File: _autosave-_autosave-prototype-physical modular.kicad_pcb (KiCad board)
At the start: 2 copper layers, 100 x 164 mm, 183 parts, among them CON1 BARREL_JACK, CON2 SD_Card_SEEEDOPL, IC1 ATMEGA2560-A, P1 POWER, P10 PC, P11 CONN_UART, P12 PJ, P15 PH, P16 PF, P18 3VI2C, P19 PIGPIO, P20 MIDI_IN, P21 MIDI_OUT, P22 BUSTI, P23 BUSTO, P3 SPI, P7 PA, Q1 BSS138, Q2 BSS138, Q3 BSS138, Q4 BSS138, Q5 BSS138, Q6 BSS138, SW1 SW_PUSH, SW10 SW_PUSH, SW11 SW_PUSH, SW12 SW_PUSH, SW13 SW_PUSH, SW14 SW_PUSH, SW2 ROTARY_ENCODER_SWITCH, SW3 SW_PUSH, SW4 SW_PUSH, SW5 SW_PUSH, SW6 SW_PUSH, SW7 SW_PUSH, SW8 SW_PUSH, SW9 SW_PUSH, U1 NCP1117ST50T3G, U2 6N138, Y1 16MHz

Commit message: new go at routing
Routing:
- net GND: track 0.00 -> 995.8 mm, vias 0 -> 29
- net +5V: track 0.00 -> 813.9 mm, vias 0 -> 44
- net /BUS_COM: track 0.00 -> 289.4 mm, vias 0 -> 3
- net /TX3: track 0.00 -> 251.4 mm, vias 0 -> 3
- net /MUXAX0: track 0.00 -> 238.7 mm, vias 0 -> 5
- net /MUXAX1: track 0.00 -> 223.4 mm, vias 0 -> 8
- net /MUXAX3: track 0.00 -> 213.7 mm, vias 0 -> 3
- net /MUXBX6: track 0.00 -> 190.4 mm, vias 0 -> 4
- net Net-(IC1-Pad65): track 0.00 -> 185.4 mm, vias 0 -> 3
- net /MUXAX2: track 0.00 -> 182.6 mm, vias 0 -> 4
- net /MUXAX4: track 0.00 -> 175.1 mm, vias 0 -> 1
- net /MUXBX5: track 0.00 -> 148.0 mm, vias 0 -> 2
- net /MUXBX4: track 0.00 -> 143.8 mm, vias 0 -> 3
- net /MUXBX1: track 0.00 -> 141.2 mm, vias 0 -> 6
- net /BUSTO_CONN: track 0.00 -> 140.0 mm, vias 0 -> 2
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
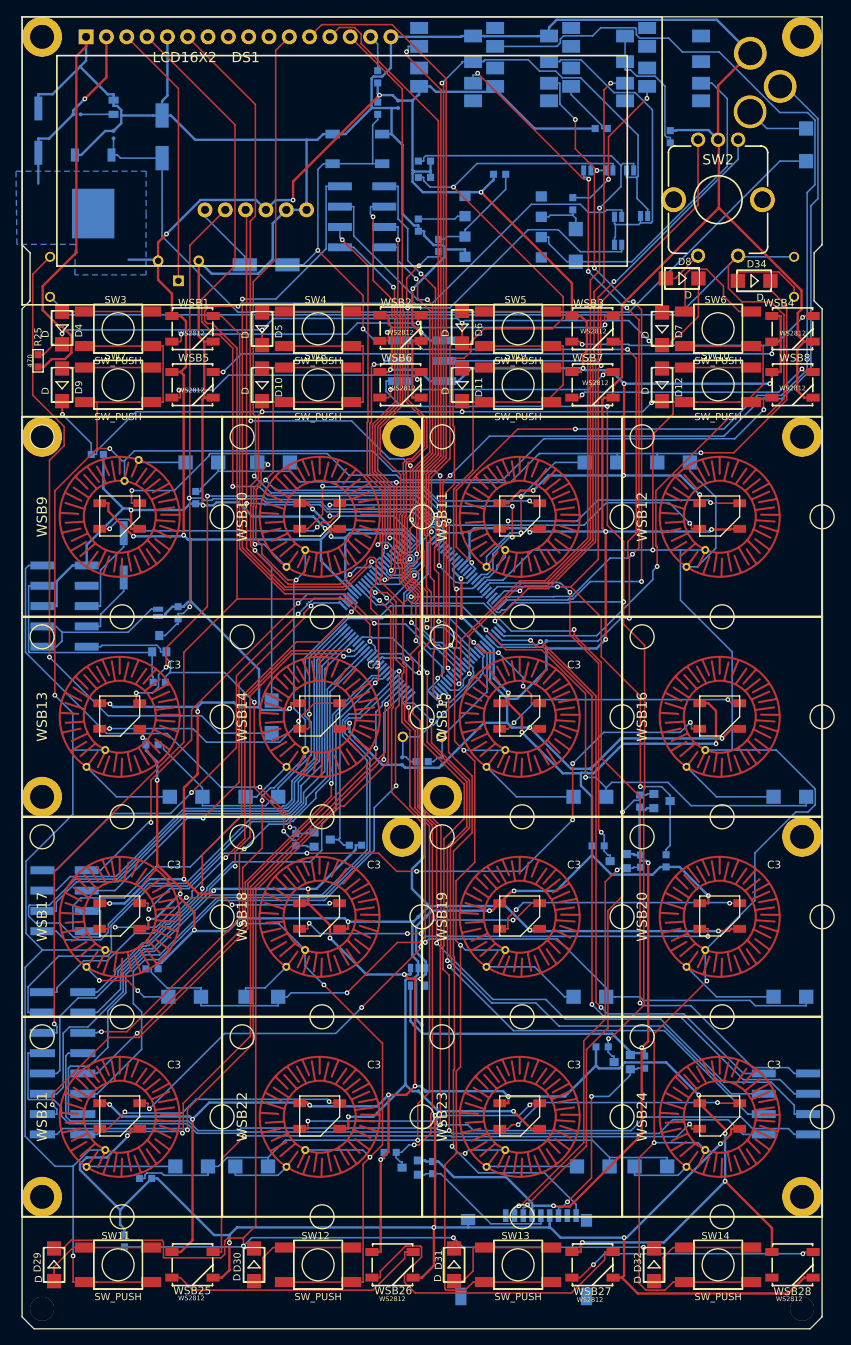
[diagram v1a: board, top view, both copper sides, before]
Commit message: move controller and hybrid firmware to virtualModular project
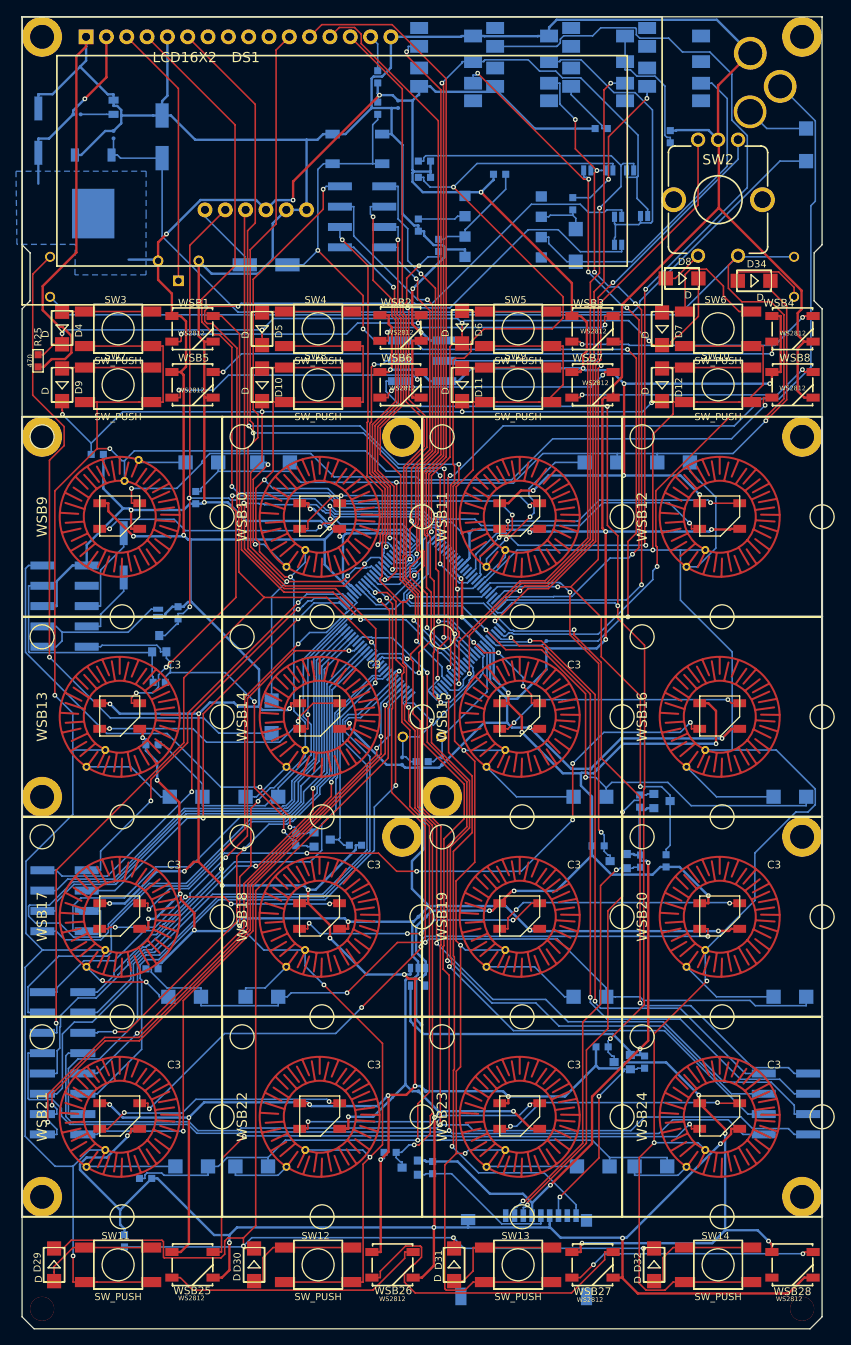
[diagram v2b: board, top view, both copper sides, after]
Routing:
- net /BUSTO_CONN: track 140.0 -> 124.6 mm
- net /PI5vRX0: track 129.9 -> 121.4 mm
- net Net-(IC1-Pad53): track 84.8 -> 78.9 mm
- net /MUXBX1: track 141.2 -> 136.2 mm
- net Net-(IC1-Pad68): track 67.0 -> 63.3 mm
- net +3V3: track 118.2 -> 114.8 mm
- net Net-(IC1-Pad91): track 75.8 -> 72.5 mm
- net /LCD1: track 103.1 -> 106.2 mm
- net GND: track 995.8 -> 993.5 mm
- net Net-(WSB10-Pad2): track 35.2 -> 33.0 mm
- net Net-(IC1-Pad65): track 185.4 -> 183.5 mm
- net +5V: track 813.9 -> 812.1 mm
- net /LCD4: track 93.1 -> 92.1 mm
- net /3vSPI_MISO: track 25.4 -> 24.3 mm
- net /POWER_IS: track 117.9 -> 116.9 mm
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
